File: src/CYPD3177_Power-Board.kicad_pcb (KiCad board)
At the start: 2 copper layers, 35.6 x 34 mm, 49 parts, among them J1 Conn_01x06, J2 USB4125-GF-A, J3 Conn_01x03, J4 Conn_01x03, J5 Conn_01x03, Q1 IRF9358PbF, Q2 BSL308PE, Q3 NTR4503N, U1 CYPD3177-24LQXQx

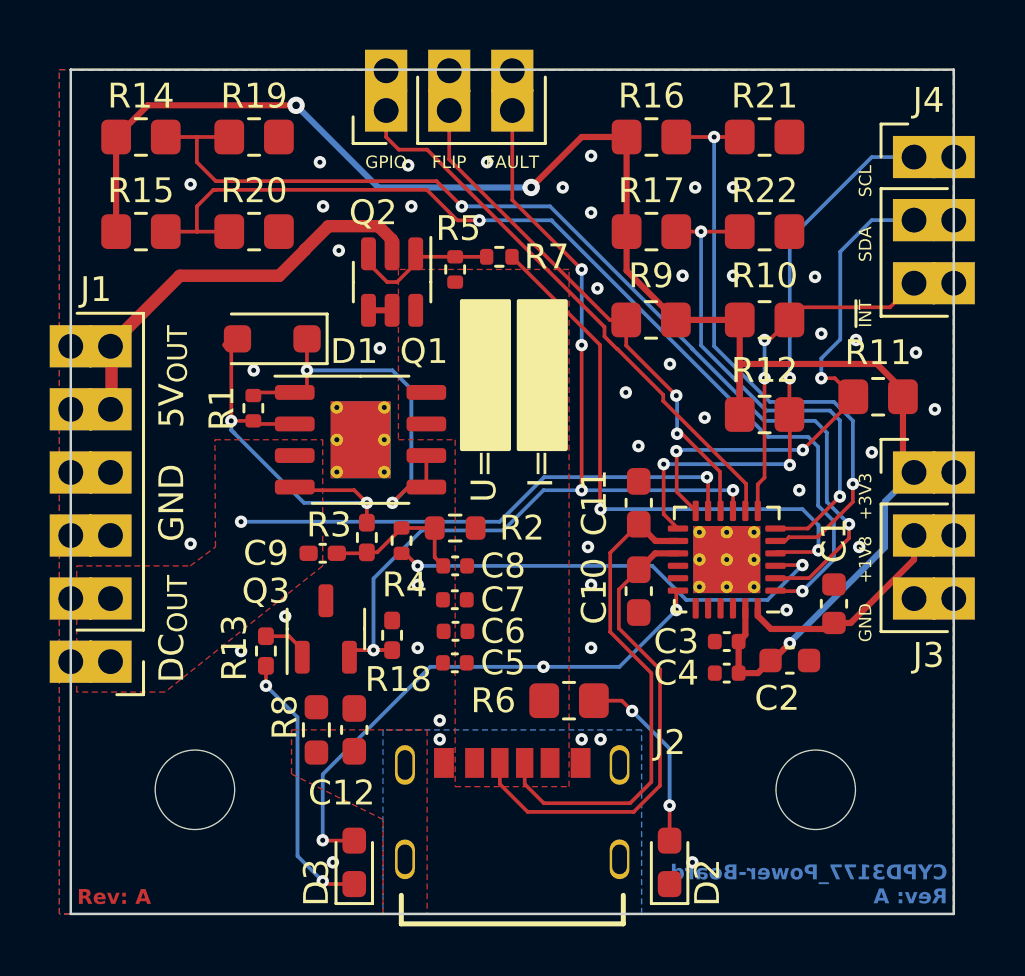
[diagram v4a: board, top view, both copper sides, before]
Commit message: Mod: PCB, removed all errors, for that the castellated holes, the USB connector and more had to be adjusted
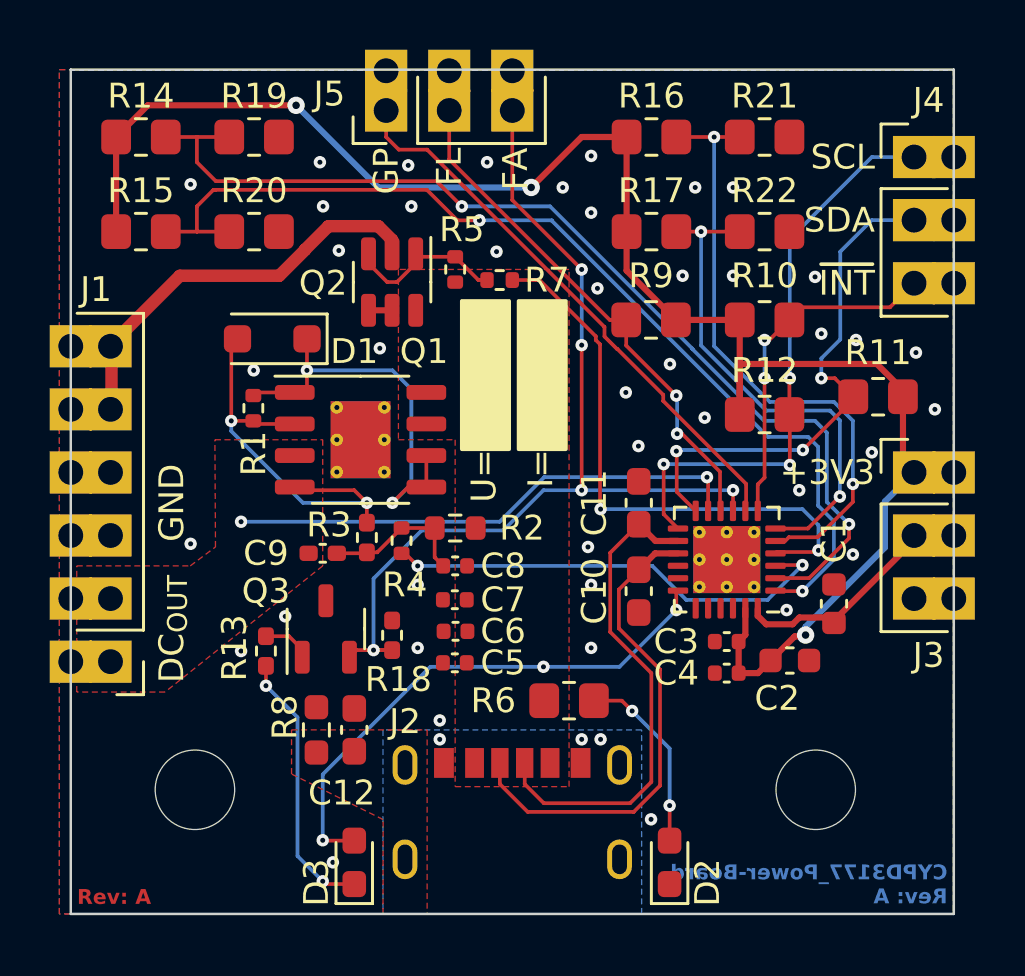
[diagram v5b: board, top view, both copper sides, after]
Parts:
- G0: footprint drawings:elektronik-emblem_3x3.5_solder -> Drawings_User:elektronik-emblem_3x3.5_solder
- moved G0 34.8 mm to (124.6, 78.7)
- moved R7 0.94 mm to (137.3, 74.5)
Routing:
- net /FET_{Gate}: track 17.2 -> 16.5 mm
- net GND: vias 44 -> 45
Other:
- board text added: "FA"
- board text added: "FL"
- board text added: "GP"
- board text removed: "+1V8"
- board text removed: "5V_{OUT}"
- board text removed: "FAULT"
- board text removed: "FLIP"
- board text removed: "GPIO"

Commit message: Add: Parts from LCSC
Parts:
- D3: value LTST-C190EKT -> LTST-C190EKT
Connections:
- Q1 pad 9: GND -> (no net)

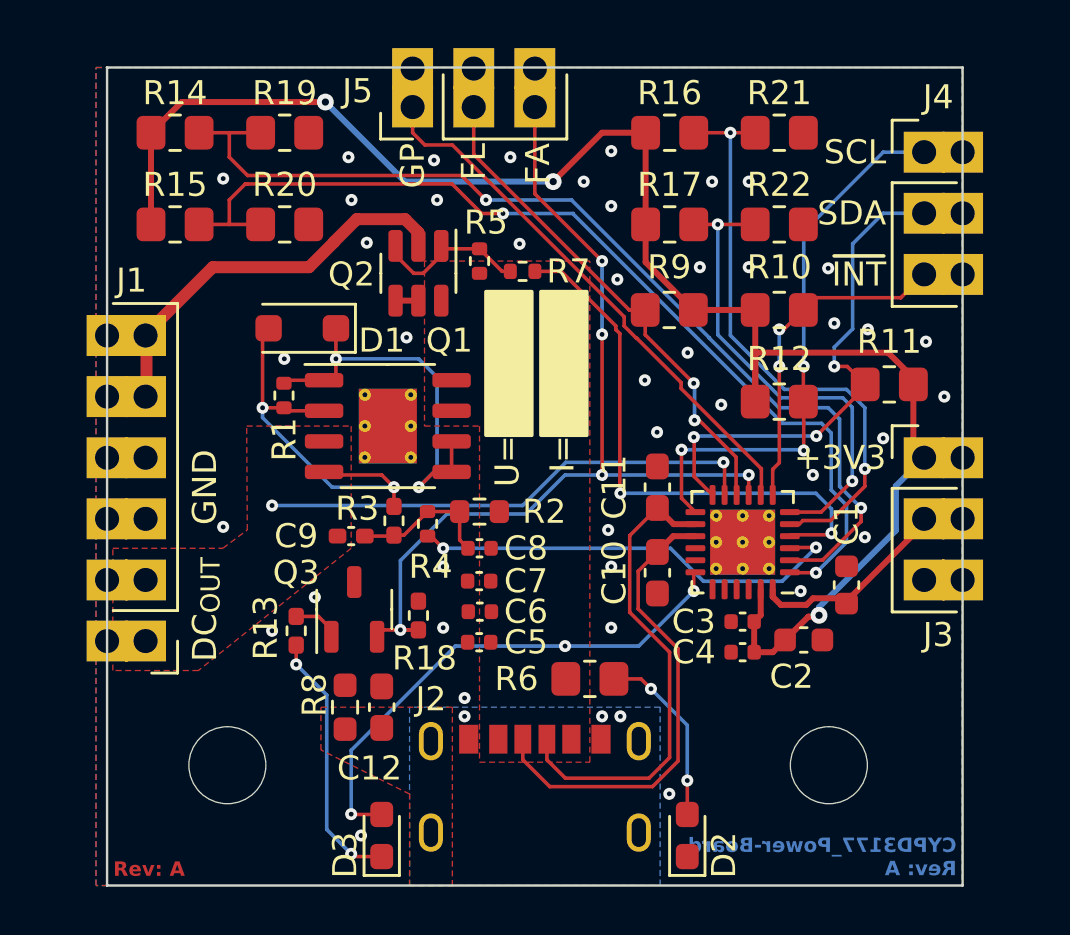
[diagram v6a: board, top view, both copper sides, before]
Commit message: Mod: Corrected the pin alignment so that the possible pin header would be on the same 2.54mm grid
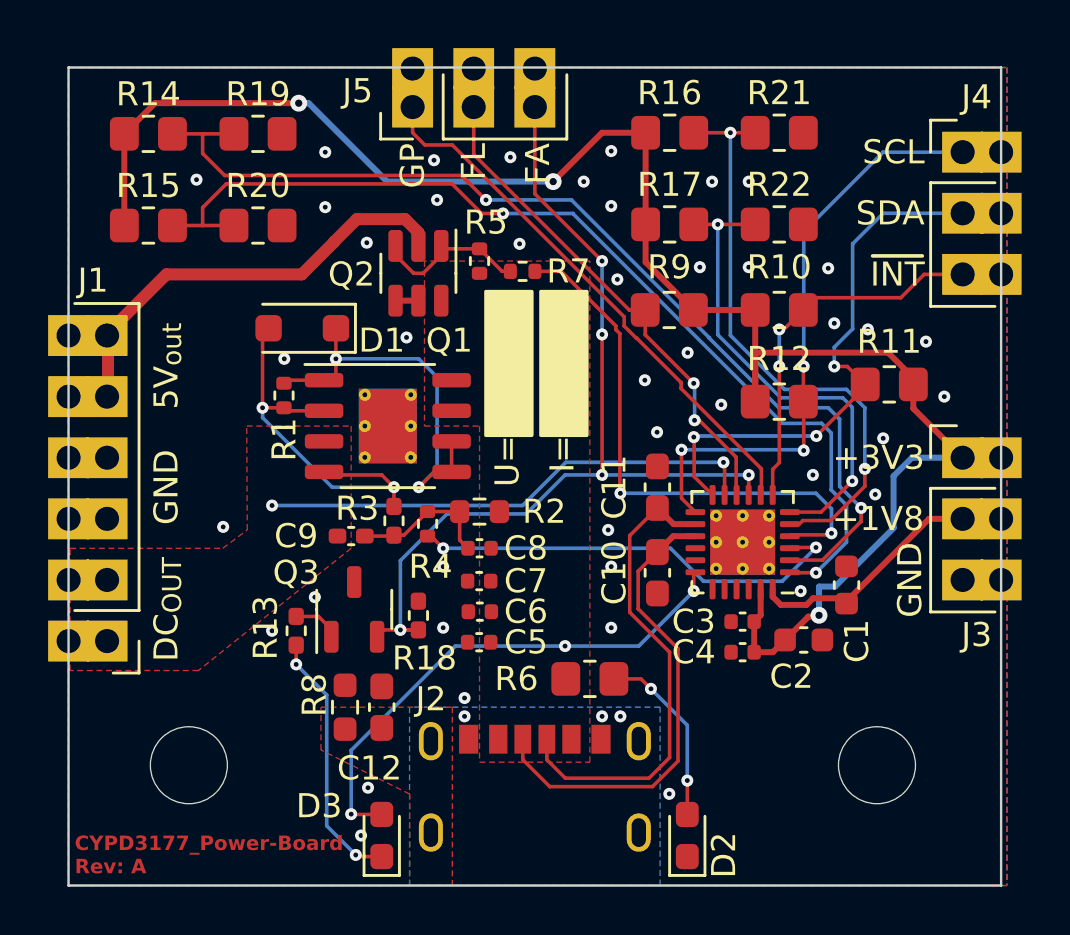
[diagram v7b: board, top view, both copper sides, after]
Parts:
- moved G0 25.7 mm to (145.9, 93.0)
- moved H2 2.00 mm to (152.0, 95.0)
- moved H1 1.60 mm to (123.4, 95.0)
- moved J1 1.60 mm to (118.4, 89.8)
- moved J3 1.60 mm to (157.2, 82.2)
- moved J4 1.60 mm to (157.2, 69.5)
- moved R19 1.11 mm to (126.3, 68.8)
- moved R20 1.11 mm to (126.3, 72.6)
- moved R14 1.11 mm to (121.7, 68.8)
- moved R15 1.11 mm to (121.7, 72.6)
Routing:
- net +3V3: track 68.7 -> 72.7 mm
- net /Safe-5V_{OUT}: track 16.7 -> 18.3 mm
- net /~{INT}: track 14.0 -> 15.6 mm
- net /SDA: track 21.3 -> 22.9 mm
- net /SCL: track 23.4 -> 25.0 mm
- net +1V8: track 8.58 -> 10.1 mm
- net /VBUS_{MAX}: track 41.7 -> 42.7 mm
- net /VBUS_{MIN}: track 40.9 -> 41.8 mm
- net GND: vias 45 -> 46
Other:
- board size 35.6 x 34 mm -> 38.8 x 34 mm
- board text added: "+1V8"
- board text added: "5V_{out}"
- board text removed: "Rev: ${REVISION}"

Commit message: Mod: Changed castellated holes to pin headers because they are cheapter
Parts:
- J1: footprint Connector_CastellatedHole_2.54mm_User:CastellatedHole_1x06_P2.54mm_PinHeaders -> Connector_PinHeader_2.54mm:PinHeader_1x06_P2.54mm_Vertical
- J3, J4, J5: footprint Connector_CastellatedHole_2.54mm_User:CastellatedHole_1x03_P2.54mm_PinHeader -> Connector_PinHeader_2.54mm:PinHeader_1x03_P2.54mm_Vertical
- moved J5 1.61 mm to (132.7, 67.7)
- moved J1 1.60 mm to (120.0, 89.8)
- moved J3 1.60 mm to (155.6, 82.2)
- moved J4 1.60 mm to (155.6, 69.5)
